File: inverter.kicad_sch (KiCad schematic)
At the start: 36 parts, among them IC3 L6498D, IC4 L6498D, IC5 L6498D, Q1 IPB320N20N3GATMA1, Q2 IPB320N20N3GATMA1, Q3 IPB320N20N3GATMA1, Q4 IPB320N20N3GATMA1, Q5 IPB320N20N3GATMA1, Q6 IPB320N20N3GATMA1

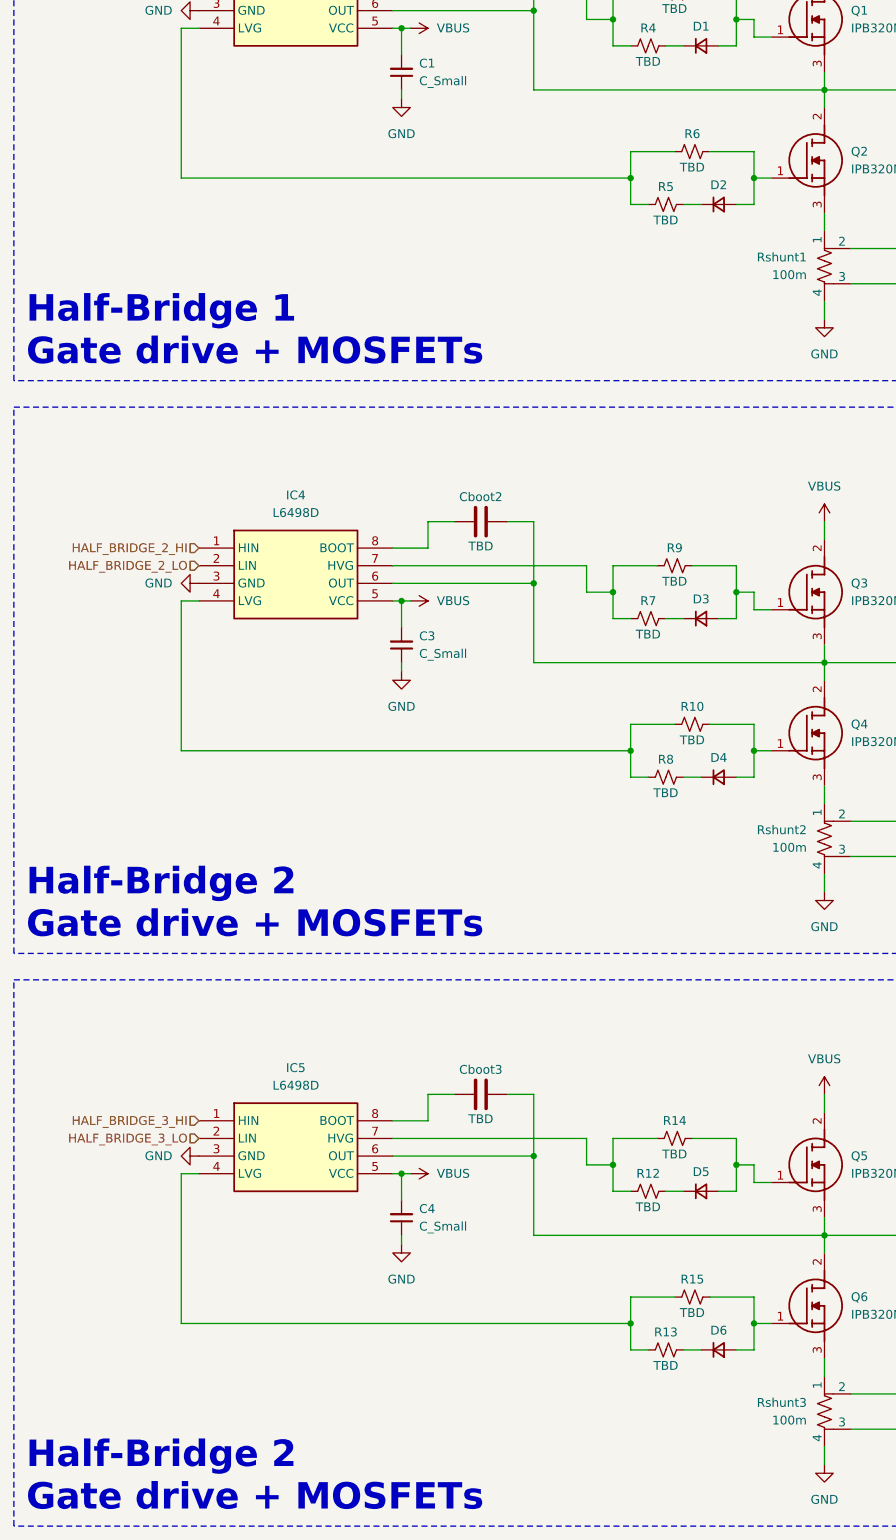
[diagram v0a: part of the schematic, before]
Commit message: Add MCU stuff, cortex debug connector and docs
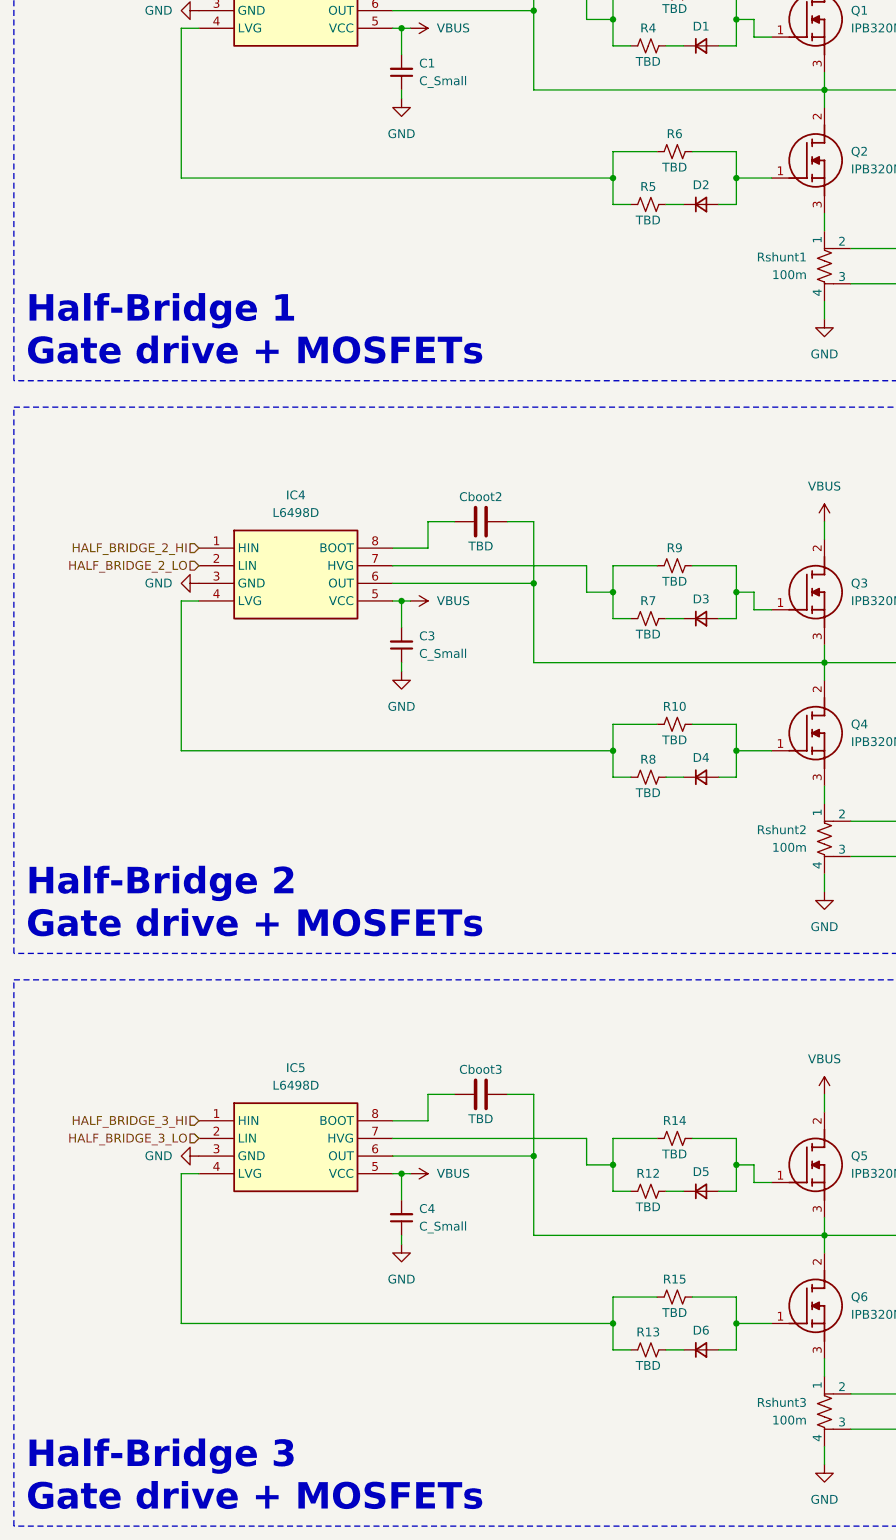
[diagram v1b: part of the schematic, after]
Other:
- note added: "Half-Bridge 3 Gate drive + MOSFETs"
- moved on the sheet: D2, D4, D6, R10, R13, R15, R5, R6, R8

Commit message: Initial routing
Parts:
- removed Q1, Q2, Q3, Q4, Q5, Q6: IPB320N20N3GATMA1, bldc-driver-pcb:IPB320N20N3GATMA1, symbol bldc-driver-pcb:IPB320N20N3GATMA1
- added J2: 43650-0303, Sandbox:43650-03YY_03040559, symbol Sandbox:43650-0303
- added J5: 2159310271, Sandbox:CONN_2159310000-SD_02_MOL, symbol Sandbox:2159310271
- added Q1, Q2, Q3, Q4, Q5, Q6: IPD320N20N3GATMA1, Sandbox:BTS3035TFATMA1, symbol bldc-driver-pcb:IPD320N20N3GATMA1
- C1, C3, C4, Cboot1, Cboot2, Cboot3: footprint (none) -> Capacitor_SMD:C_0603_1608Metric
- R10, R12, R13, R14, R15, R2, R4, R5, R6, R7, R8, R9: footprint (none) -> Resistor_SMD:R_0603_1608Metric
- Rshunt1, Rshunt2, Rshunt3: footprint (none) -> Resistor_SMD:R_0805_2012Metric
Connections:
- net GND: now also J5.2_1, J5.2_2
- net HALF_BRIDGE_1_OUT: now also J2.2, Q1.3 (S), Q2.2 (D); no longer Cboot2.2, Cboot3.2, IC4.6 (OUT), IC5.6 (OUT)
- net VBUS: now also J5.1_1, J5.1_2, Q1.2 (D), Q3.2 (D), Q5.2 (D)
- net at D4.2 (A), R10.2: now also Q4.1 (G)
- net at Rshunt2.1: now also Q4.3 (S)
- net at D1.2 (A), R2.2: now also Q1.1 (G)
- net at D3.2 (A), R9.2: now also Q3.1 (G)
- net at D2.2 (A), R6.2: now also Q2.1 (G)
- net at D6.2 (A), R15.2: now also Q6.1 (G)
- net at D5.2 (A), R14.2: now also Q5.1 (G)
- net at Rshunt1.1: now also Q2.3 (S)
- net at Rshunt3.1: now also Q6.3 (S)
- new net HALF_BRIDGE_2_OUT: Cboot2.2, IC4.6 (OUT), J2.1, Q3.3 (S), Q4.2 (D)
- new net HALF_BRIDGE_3_OUT: Cboot3.2, IC5.6 (OUT), J2.3, Q5.3 (S), Q6.2 (D)
- no-connect marks 0 -> 2

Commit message: More routing
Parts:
- removed Rshunt1, Rshunt2, Rshunt3: 100m, Resistor_SMD:R_0805_2012Metric, symbol Device:R_Shunt_US
- added R31, R32, R33, R34, R35, R36: 10k, Resistor_SMD:R_0603_1608Metric, symbol Device:R_US
- added Rshunt1, Rshunt2, Rshunt3: 100m, Resistor_SMD:R_1206_3216Metric, symbol Device:R_US
- D1, D2, D3, D4, D5, D6: footprint (none) -> Diode_SMD:D_0603_1608Metric
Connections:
- net CSA_1_IN+: now also Q2.3 (S), Rshunt1.1
- net CSA_2_IN+: now also Q4.3 (S), Rshunt2.1
- net CSA_3_IN+: now also Q6.3 (S), Rshunt3.1
- net GND: now also R31.2, R32.2, R33.2, R34.2, R35.2, R36.2, Rshunt1.2, Rshunt2.2, Rshunt3.2
- net at D1.2 (A), Q1.1 (G), R2.2: now also R31.1
- net at D3.2 (A), Q3.1 (G), R9.2: now also R33.1
- net at D2.2 (A), Q2.1 (G), R6.2: now also R32.1
- net at D6.2 (A), Q6.1 (G), R15.2: now also R36.1
- net at D4.2 (A), Q4.1 (G), R10.2: now also R34.1
- net at D5.2 (A), Q5.1 (G), R14.2: now also R35.1
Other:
- moved on the sheet: D1, D3, D5, Q1, Q2, Q3, Q4, Q5, Q6, R12, R14, R2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

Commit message: Finalize layout -- VREF pending
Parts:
- removed J2: 43650-0303, Sandbox:43650-03YY_03040559, symbol Sandbox:43650-0303
- removed J5: 2159310271, Sandbox:CONN_2159310000-SD_02_MOL, symbol Sandbox:2159310271
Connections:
- no-connect marks 2 -> 0

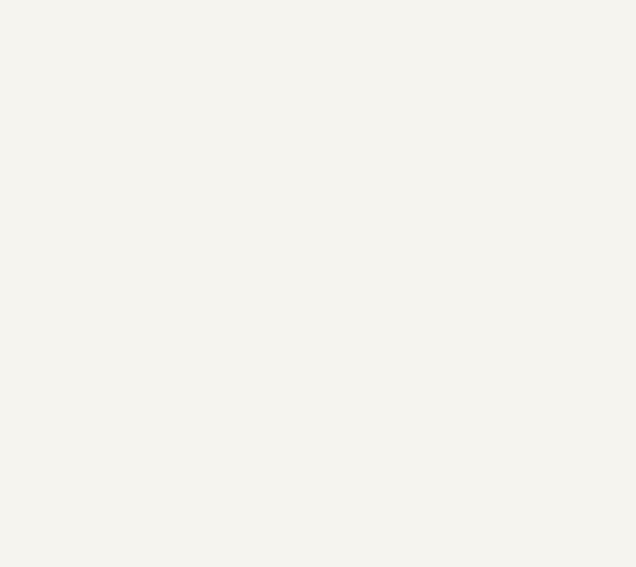
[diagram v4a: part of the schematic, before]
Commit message: Add connector for motor phases
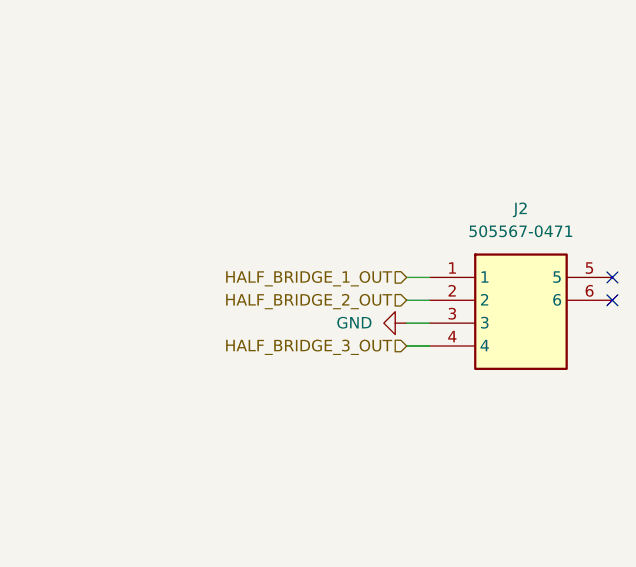
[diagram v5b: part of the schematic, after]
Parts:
- added J2: 505567-0471, bldc-driver-pcb:5055670471, symbol bldc-driver-pcb:505567-0471
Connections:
- net GND: now also J2.3
- net HALF_BRIDGE_1_OUT: now also J2.1
- net HALF_BRIDGE_2_OUT: now also J2.2
- net HALF_BRIDGE_3_OUT: now also J2.4
- no-connect marks 0 -> 2
